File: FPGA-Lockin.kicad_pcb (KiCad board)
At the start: 4 copper layers, 48.8 x 55.2 mm, 116 parts, among them J1 SPI Header, J2 G125-MH104M4-04AD000P, J3 Laser, J4 PZT, J5 Micro_SD_Card, J6 Conn_02x07_Odd_Even, J7 Conn_01x02_Pin, U1 ICE40UP5K-SG48ITR, U10 OPA310xDBV, U11 MCP1501-30xSN, U12 MCP3561R-E/ST, U13 AD5761RBRUZ-RL7, U14 MIC94090YC6, U15 MCP2562, U2 INA180, U3 SPX3819M5-L-1-2, U4 SPX3819M5-L-2-5, U5 LMR64010XMF, U6 SPX3819M5-L-3-3, U7 STM32F405RGTx, U8 MCP1754S-3302xCB, U9 W25Q32JVSS, Y1 Crystal_GND24

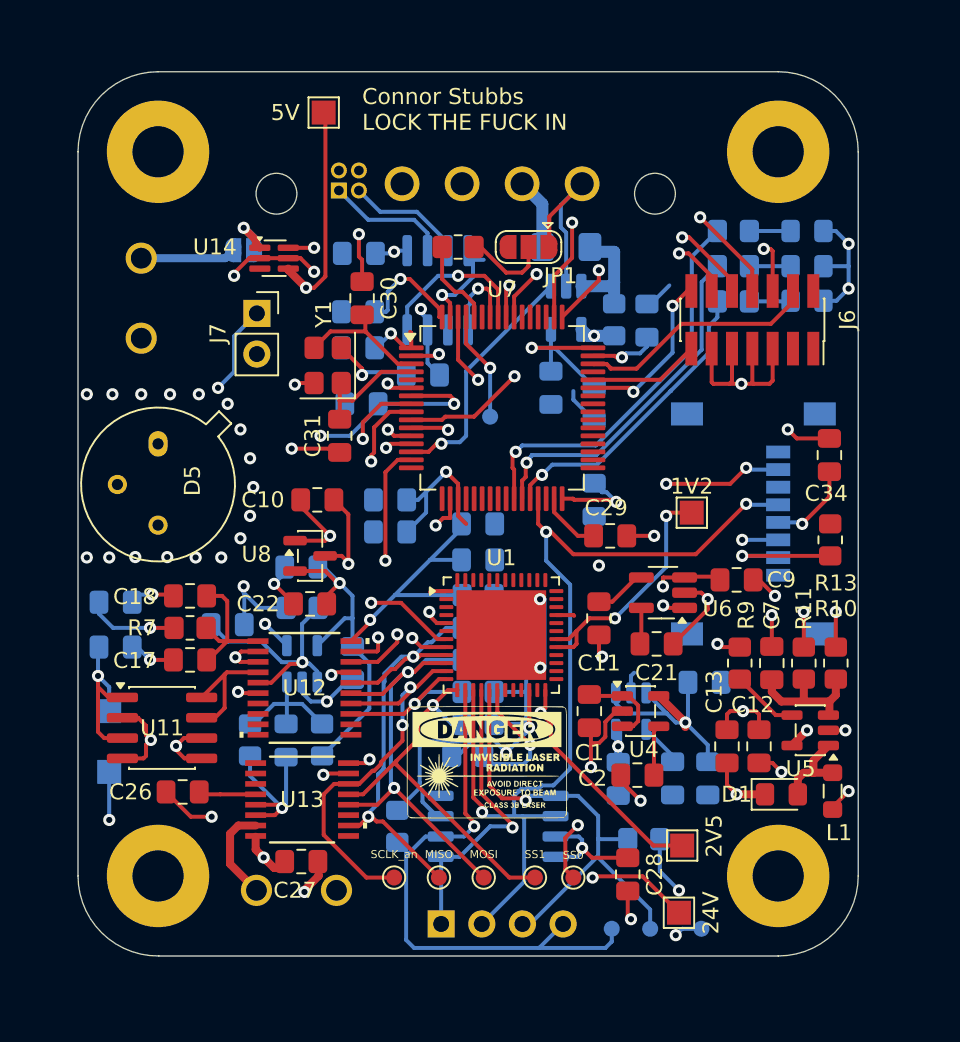
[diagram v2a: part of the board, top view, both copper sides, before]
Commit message: Fix layout errors after reviewing
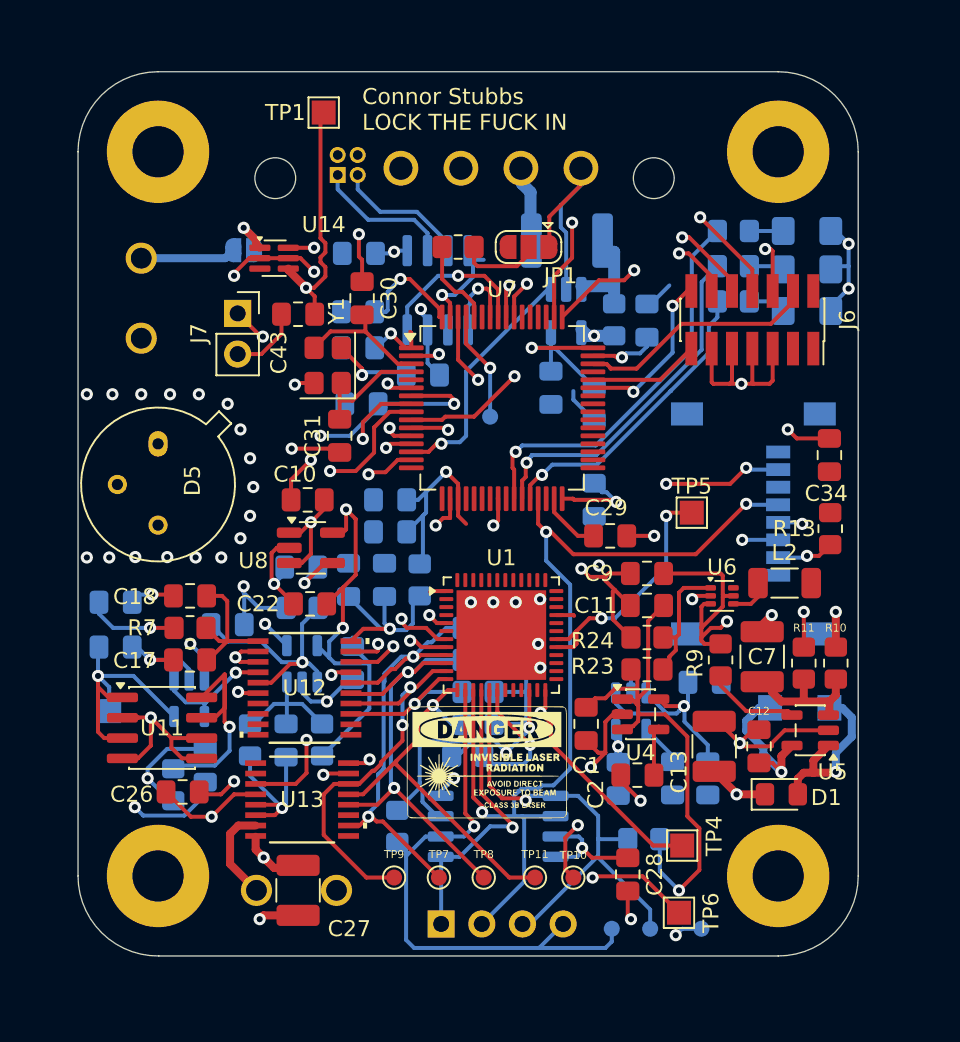
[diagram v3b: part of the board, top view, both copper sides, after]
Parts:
- removed 3V3: 3V3D, TestPoint:TestPoint_Pad_1.5x1.5mm
- removed C21: 1uF, Capacitor_SMD:C_0805_2012Metric_Pad1.18x1.45mm_HandSolder
- added C43: 0.1uF, Capacitor_SMD:C_0805_2012Metric_Pad1.18x1.45mm_HandSolder, F.Cu at (126.0, 50.4)
- added C44: 10uF, Capacitor_SMD:C_0805_2012Metric_Pad1.18x1.45mm_HandSolder, B.Cu at (120.2, 78.6)
- added L2: 1uH, Inductor_SMD:L_1206_3216Metric_Pad1.22x1.90mm_HandSolder, F.Cu at (156.4, 67.2)
- added R15: 10kR, Resistor_SMD:R_0805_2012Metric_Pad1.20x1.40mm_HandSolder, B.Cu at (118.2, 79.8)
- added R23: 453kR, Resistor_SMD:R_0805_2012Metric_Pad1.20x1.40mm_HandSolder, F.Cu at (147.8, 72.6)
- added R24: 100kR, Resistor_SMD:R_0805_2012Metric_Pad1.20x1.40mm_HandSolder, F.Cu at (147.8, 70.6)
- added U16: OPA310xDBV, Package_TO_SOT_SMD:SOT-23-5, B.Cu at (119.2, 74.4)
- C10: value 0.1uF -> 1uF
- C11: value 10nF -> 22uF
- C13, C27, C7: footprint Capacitor_SMD:C_0805_2012Metric_Pad1.18x1.45mm_HandSolder -> Capacitor_SMD:C_1210_3225Metric_Pad1.33x2.70mm_HandSolder
- C20: value 0.1uF -> 10nF
- C22: value 10uF -> 1uF
- C30, C31: value 27pF -> 10pF
- C9: value 1uF -> 4.7uF
- D2, D3, D4: footprint LED_SMD:LED_0805_2012Metric_Pad1.15x1.40mm_HandSolder -> LED_SMD:LED_1206_3216Metric_Pad1.42x1.75mm_HandSolder
- F1: value 2A Polyfuse -> 0ZCG0075FF2C; footprint Fuse:Fuse_1206_3216Metric_Pad1.42x1.75mm_HandSolder -> Fuse:Fuse_1812_4532Metric_Pad1.30x3.40mm_HandSolder
- L1: value 12uH -> CC453232-120KL; footprint Inductor_SMD:L_0805_2012Metric_Pad1.05x1.20mm_HandSolder -> ind:IND_BOURNS_CC453232; moved to B.Cu
- R12: value 16mR -> 25mR
- U6: value SPX3819M5-L-3-3 -> TLV62568ADRL; footprint Package_TO_SOT_SMD:SOT-23-5_HandSoldering -> Package_TO_SOT_SMD:SOT-563
- U8: value MCP1754S-3302xCB -> SPX3819M5-L-3-3; footprint Package_TO_SOT_SMD:SOT-23 -> Package_TO_SOT_SMD:SOT-23-5_HandSoldering
- Y1: value Crystal_GND24 -> ABM8G
- moved C24 8.82 mm to (129.2, 67.0), turned to -90 degrees
- moved C25 5.98 mm to (131.4, 67.0), turned to -90 degrees
- moved C9 5.61 mm to (147.8, 66.6), turned to 180 degrees
- moved L1 5.59 mm to (157.3, 75.0), turned to 180 degrees
- moved R8 3.77 mm to (133.6, 67.0), turned to -90 degrees
- moved U6 3.69 mm to (152.5, 68.0), turned to 0 degrees
- moved C11 3.10 mm to (147.8, 68.6), turned to 180 degrees
- moved C27 1.81 mm to (126.0, 86.4), turned to -90 degrees
- moved R9 1.22 mm to (152.4, 72.0)
- moved J7 1.20 mm to (122.2, 50.4)
- moved J2 0.97 mm to (136.4, 38.2)
- moved C1 0.82 mm to (144.0, 76.0)
- moved C13 0.80 mm to (152.0, 77.4)
- moved C7 0.72 mm to (155.0, 71.8)
- moved R13 0.70 mm to (159.2, 63.8)
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- renumbered 3V3A to 3.3VA, 5V to TP1, SS0 to TP10, SS1 to TP11, MOSI to TP12, MISO to TP13, SS0 to TP14, SCLK_m to TP15, 2V5 to TP4, 1V2 to TP5, 24V to TP6, MISO to TP7, MOSI to TP8, SCLK_an to TP9
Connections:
- net /SS0_an renamed /~{SS0_an}
- net /SS0_mem renamed /~{SS0_mem}
- net /SS1_an renamed /~{SS1_an}
- net /SS1_mem renamed /~{SS1_mem}
- C11 pad 1: Net-(U6-BP) -> +3V3
- C20 pad 1: +3.3VA -> Net-(U8-BP)
- C26 pad 2: Net-(U13-VREFIN/VREFOUT) -> GND
- L1 pad 1: +5V -> Net-(D1-A)
- L1 pad 2: Net-(D1-A) -> +5V
- U12 pad 4: Net-(U11-FB) -> Net-(U12-REFIN+/OUT)
- U13 pad 3: unconnected-(U13-*RESET-Pad3) -> /DAC_RST
- U13 pad 4: Net-(U13-VREFIN/VREFOUT) -> +2V5
- U6 pad 1: +5V -> Net-(U6-FB)
- U6 pad 4: Net-(U6-BP) -> Net-(U6-SW)
- U6 pad 5: +3V3 -> +5V
- U7 pad 24: unconnected-(U7-PC4-Pad24) -> /DAC_RST
- U8 pad 1: GNDA -> +5V
- U8 pad 2: +3.3VA -> GNDA
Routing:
- net /DAC_RST: track 0.00 -> 30.1 mm, vias 0 -> 2
- net GND: track 104.7 -> 134.8 mm, vias 20 -> 25
- net Net-(U16-+): track 0.00 -> 19.0 mm, vias 0 -> 2
- net GNDA: track 64.0 -> 83.0 mm, vias 33 -> 32
- net +5V: track 48.0 -> 64.3 mm, vias 13 -> 9
- net +3V3: track 106.5 -> 121.4 mm, vias 12 -> 11
- net +3.3VA: track 71.1 -> 81.0 mm, vias 4 -> 5
- net Net-(U6-FB): track 0.00 -> 8.35 mm
- net Net-(U12-REFIN+/OUT): track 0.00 -> 7.92 mm, vias 0 -> 1
- net Net-(U11-FB): track 7.96 -> 14.7 mm, vias 0 -> 1
- net Net-(D1-A): track 5.80 -> 11.5 mm, vias 0 -> 1
- net Net-(U12-DVDD): track 16.3 -> 11.9 mm
- net /CDONE: track 19.4 -> 23.7 mm
- net Net-(J7-Pin_1): track 26.1 -> 22.4 mm
- net Net-(U13-VREFIN/VREFOUT): track 3.67 -> 0.00 mm
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
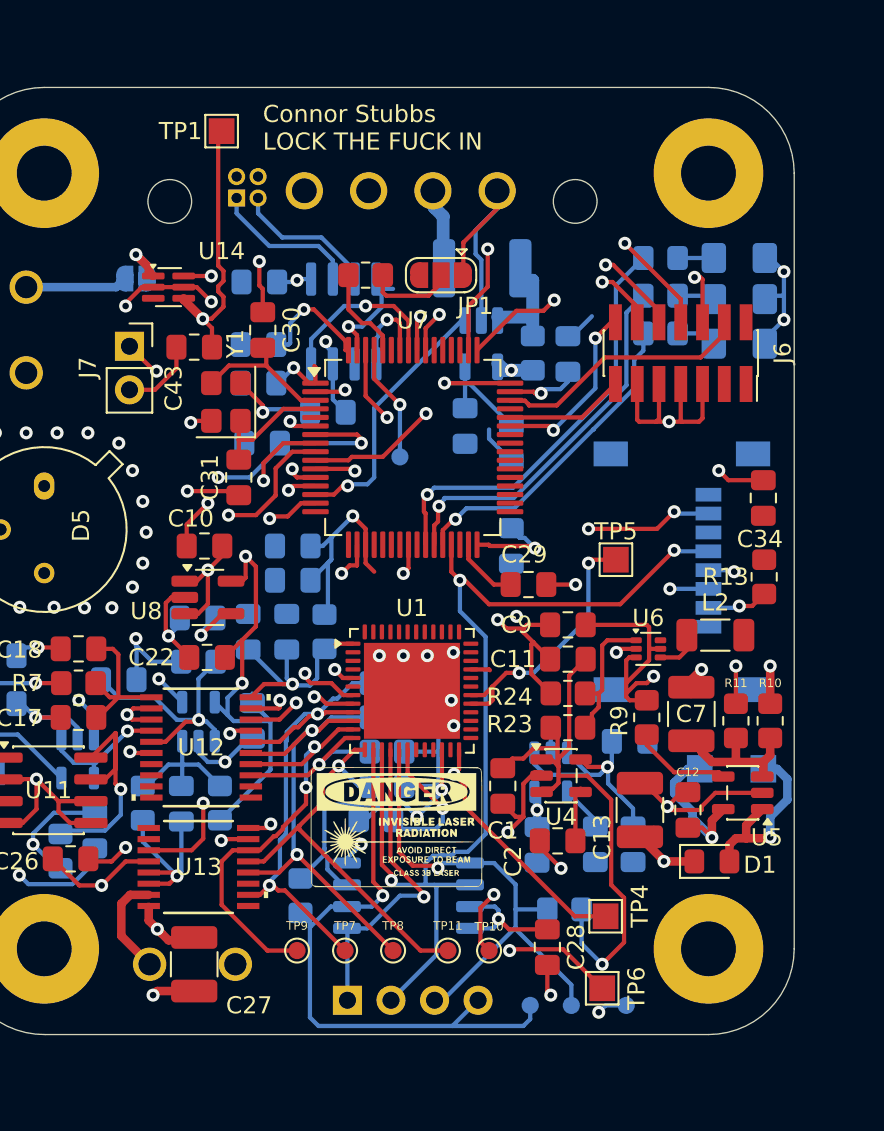
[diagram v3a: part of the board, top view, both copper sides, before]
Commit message: Fix diode
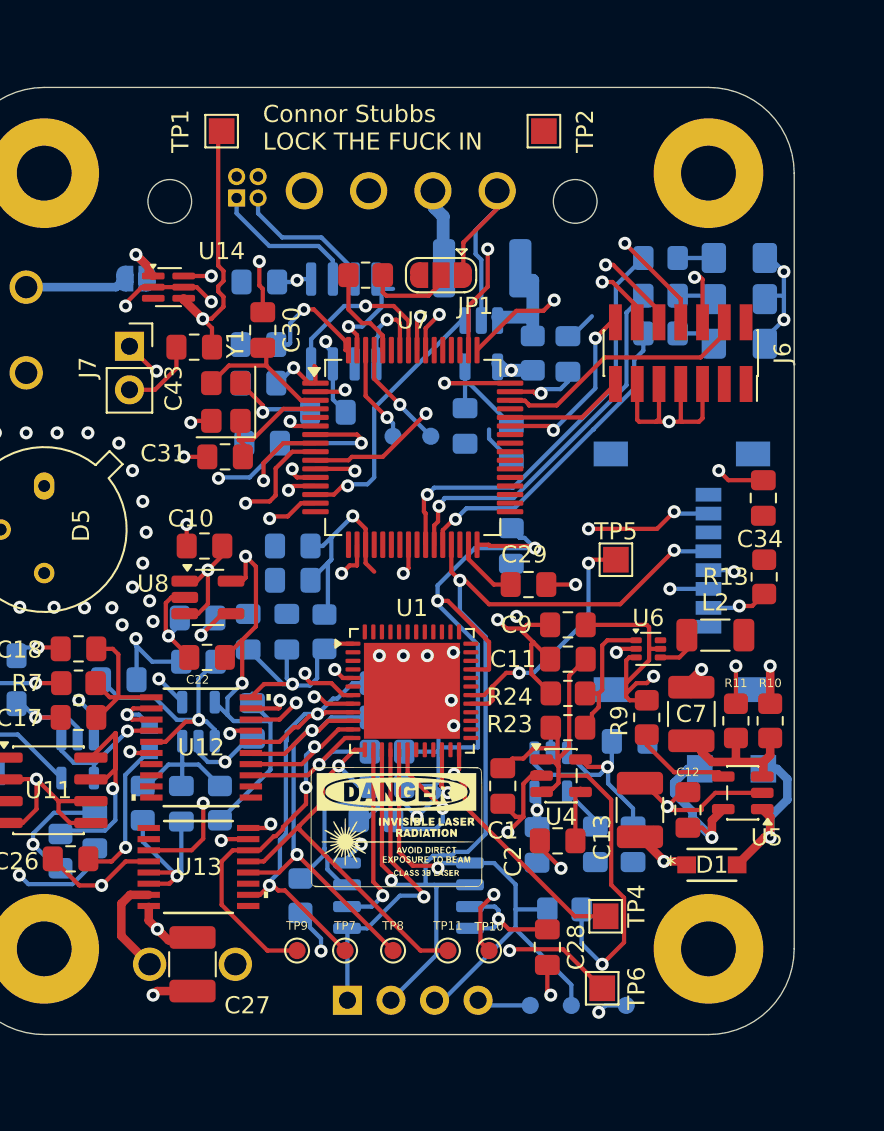
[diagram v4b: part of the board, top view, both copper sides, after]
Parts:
- added FL1: BLM18PG121SN1D, fer:BEADC1608X95N, B.Cu at (123.4, 73.2)
- added TP2: 3V3, TestPoint:TestPoint_Pad_1.5x1.5mm, F.Cu at (146.4, 37.8)
- added TPS1_m1: SS1_mem, TestPoint:TestPoint_Pad_D1.0mm, B.Cu at (137.6, 55.6)
- D1: footprint Diode_SMD:D_0805_2012Metric_Pad1.15x1.40mm_HandSolder -> dio:DIO_RB051MM_ROM
- moved TP14 2.16 mm to (139.8, 55.6)
- moved C31 1.44 mm to (127.8, 56.8), turned to 0 degrees
- moved D1 0.20 mm to (156.2, 80.6)
- moved C27 0.10 mm to (125.9, 86.4)
- renumbered 3.3VA to TP3
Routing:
- net +3V3: track 121.4 -> 147.2 mm, vias 11 -> 12
- net GND: track 134.8 -> 149.5 mm
- net /MISO_mem: track 99.8 -> 93.7 mm, vias 4 -> 5
- net Net-(D1-A): track 11.5 -> 10.1 mm
- net /~{SS1_mem}: track 33.1 -> 34.4 mm
- net GNDA: track 83.0 -> 82.9 mm, vias 32 -> 35
